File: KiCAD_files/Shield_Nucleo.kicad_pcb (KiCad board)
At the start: 4 copper layers, 100 x 100 mm, 113 parts, among them J1 Conn_01x02, J2 RJ45_LED_Shielded, J3 RJ45_LED_Shielded, J4 Conn_01x02_Male, J5 Conn_01x04_Male, J6 Conn_01x02, J8 Conn_02x07_Odd_Even, SW1 SW_Push, U1 STM32G474RE, U2 AT25xxx, U3 TCAN334GDR, U4 AP1117-33, U5 UCC21222DR, U6 UCC21222DR, U7 SFH617A-2X009T, Y1 NX3225SA-16.000000MHZ-T1

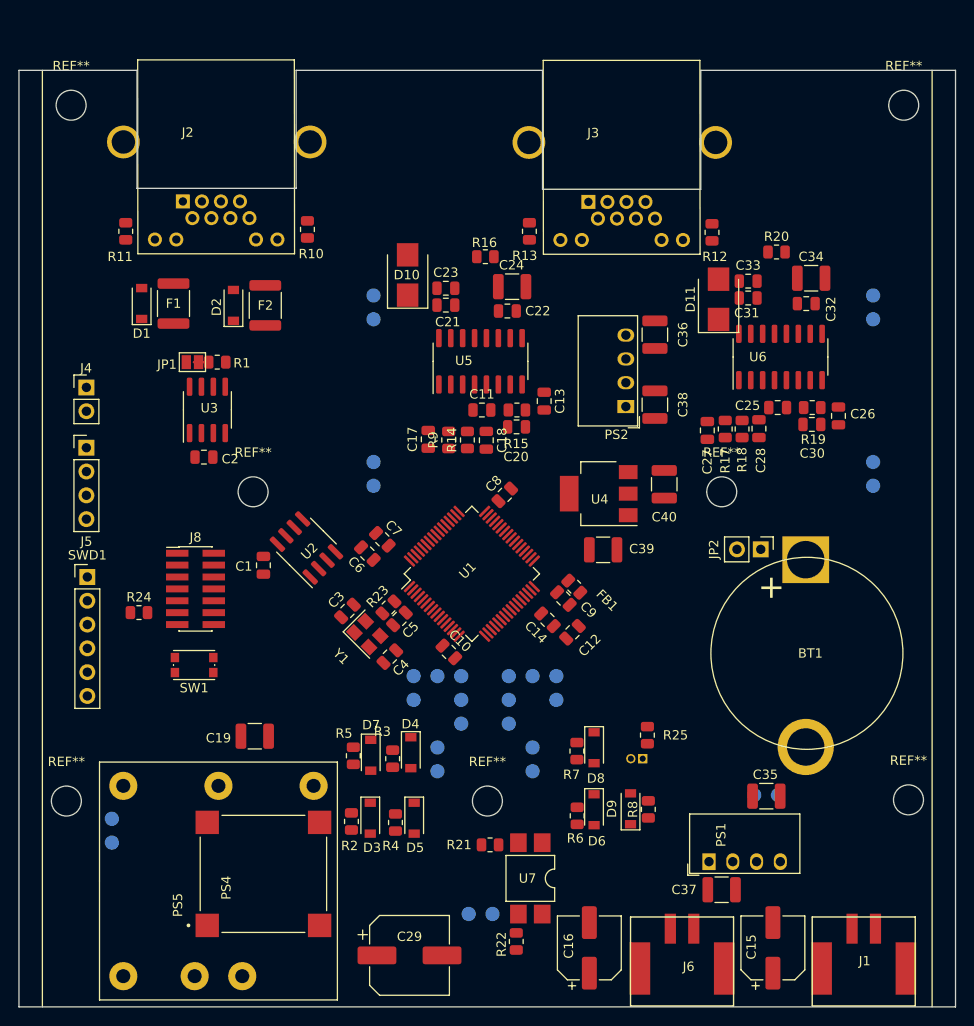
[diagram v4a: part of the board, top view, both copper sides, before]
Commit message: WIP: nearly finished routing - Power need via stiching Signal miss test points connections.
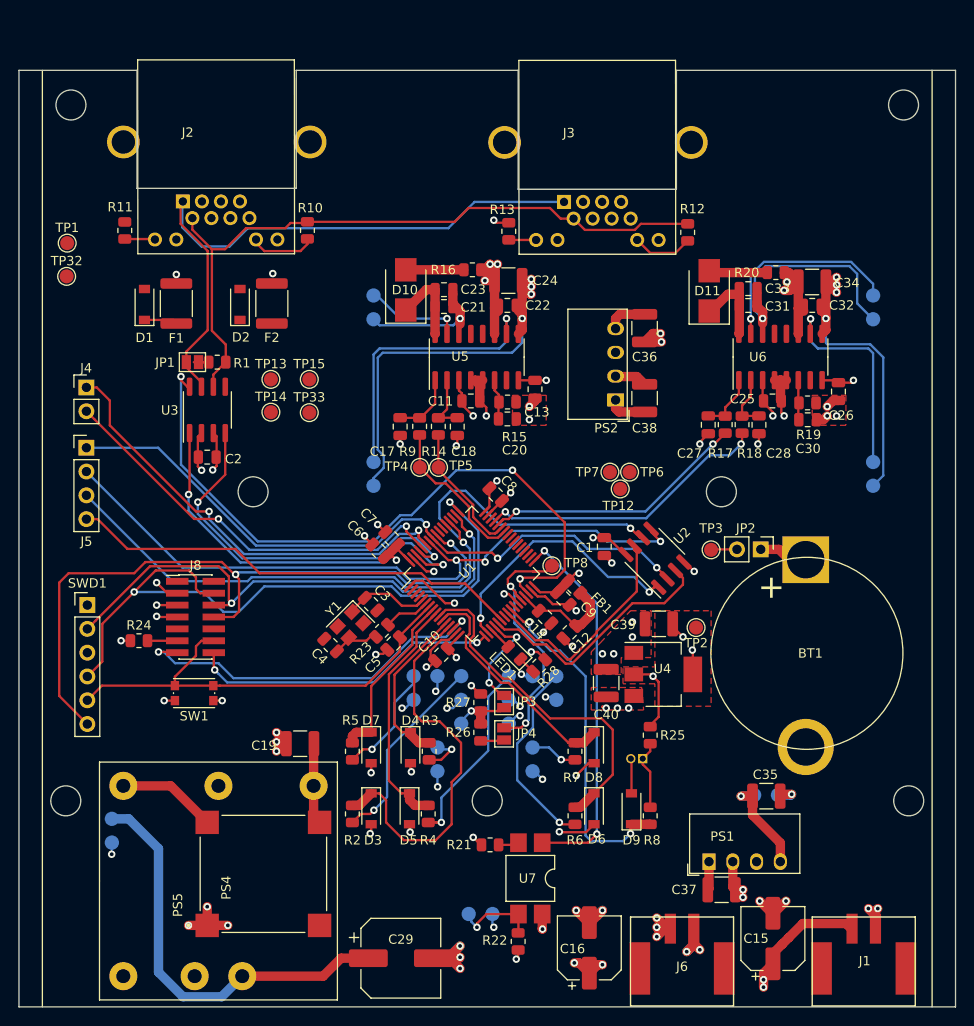
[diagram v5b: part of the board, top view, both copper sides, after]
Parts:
- removed 3D1: 3D_Footprint, Footprints:3D_Footprint_Power
- removed the REF** at (88.5, 104.5)
- removed the REF** at (43.6, 104.5)
- removed the REF** at (113.5, 71.5)
- removed the REF** at (63.5, 71.5)
- removed the REF** at (44.1, 30.2)
- removed the REF** at (133.0, 30.2)
- removed the REF** at (133.5, 104.4)
- added J7: Power, Footprints:3D_Footprint_Power, F.Cu at (38.5, 26.5)
- added JP3: SolderJumper_2_Open, Jumper:SolderJumper-2_P1.3mm_Open_Pad1.0x1.5mm, F.Cu at (90.3, 93.9)
- added JP4: SolderJumper_2_Open, Jumper:SolderJumper-2_P1.3mm_Open_Pad1.0x1.5mm, F.Cu at (90.3, 97.3)
- added LED1: LED, LED_SMD:LED_0805_2012Metric, F.Cu at (91.4, 88.7)
- added R26: 100K, Resistor_SMD:R_0805_2012Metric, F.Cu at (87.8, 97.2)
- added R27: 100K, Resistor_SMD:R_0805_2012Metric, F.Cu at (87.8, 94.0)
- added R28: 330, Resistor_SMD:R_0805_2012Metric, F.Cu at (94.0, 90.1)
- added TP1: TestPoint, TestPoint:TestPoint_Pad_D1.5mm, F.Cu at (43.6, 45.0)
- added TP12: TestPoint, TestPoint:TestPoint_Pad_D1.5mm, F.Cu at (102.7, 71.2)
- added TP13: TestPoint, TestPoint:TestPoint_Pad_D1.5mm, F.Cu at (65.4, 59.5)
- added TP14: TestPoint, TestPoint:TestPoint_Pad_D1.5mm, F.Cu at (65.4, 63.0)
- added TP15: TestPoint, TestPoint:TestPoint_Pad_D1.5mm, F.Cu at (69.5, 59.5)
- added TP2: TestPoint, TestPoint:TestPoint_Pad_D1.5mm, F.Cu at (110.8, 86.0)
- added TP3: TestPoint, TestPoint:TestPoint_Pad_D1.5mm, F.Cu at (112.4, 77.7)
- added TP32: TestPoint, TestPoint:TestPoint_Pad_D1.5mm, F.Cu at (43.6, 48.5)
- added TP33: TestPoint, TestPoint:TestPoint_Pad_D1.5mm, F.Cu at (69.5, 63.0)
- added TP4: TestPoint, TestPoint:TestPoint_Pad_D1.5mm, F.Cu at (81.3, 68.9)
- added TP5: TestPoint, TestPoint:TestPoint_Pad_D1.5mm, F.Cu at (83.3, 68.9)
- added TP6: TestPoint, TestPoint:TestPoint_Pad_D1.5mm, F.Cu at (103.7, 69.4)
- added TP7: TestPoint, TestPoint:TestPoint_Pad_D1.5mm, F.Cu at (101.6, 69.4)
- added TP8: TestPoint, TestPoint:TestPoint_Pad_D1.5mm, F.Cu at (95.4, 79.4)
- moved U2 37.2 mm to (106.4, 78.6)
- moved C1 36.5 mm to (101.0, 77.3)
- moved C40 22.1 mm to (101.2, 91.9)
- moved U4 20.5 mm to (107.3, 91.0), turned to 0 degrees
- moved C39 9.89 mm to (106.8, 85.6), turned to 180 degrees
- moved C4 6.45 mm to (71.8, 87.9), turned to 135 degrees
- moved C19 4.92 mm to (68.5, 98.4)
- moved R3 3.98 mm to (82.3, 99.2)
- moved R4 3.62 mm to (82.2, 105.9)
- moved C18 3.43 mm to (85.3, 64.5)
- moved R14 3.42 mm to (83.3, 64.5)
- moved R9 3.42 mm to (81.3, 64.5)
- moved C17 3.29 mm to (79.2, 64.5)
- moved J8 3.00 mm to (57.4, 84.9)
- moved R24 3.00 mm to (51.3, 87.4)
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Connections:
- net /HRTIM1_CHC1 renamed Net-(U1-Pad34)
- net /HRTIM1_CHC2 renamed Net-(U1-Pad35)
- net /HRTIM1_CHD1 renamed Net-(U1-Pad36)
- net /HRTIM1_CHD2 renamed Net-(U1-Pad37)
- net /HRTIM1_CHE1 renamed Net-(U1-Pad40)
- net /HRTIM1_CHE2 renamed Net-(U1-Pad41)
- net /HRTIM1_CHF1 renamed Net-(U1-Pad38)
- net /HRTIM1_CHF2 renamed Net-(U1-Pad39)
- C15 pad 1: Net-(C15-Pad1) -> /+12VD
- C16 pad 1: Net-(C16-Pad1) -> +12V
- J1 pad 1: Net-(C15-Pad1) -> /+12VD
- J6 pad 1: Net-(C16-Pad1) -> +12V
- PS5 pad 1: Net-(PS5-Pad1) -> /+12VD
- U1 pad 11: /EEPROM_WP -> /V_high_mcu
- U1 pad 13: /V2_low_mcu -> /I1_low_mcu
- U1 pad 19: /V_high_mcu -> /LED_BUILTIN
- U1 pad 20: Net-(U1-Pad20) -> /DAC2
- U1 pad 21: Net-(U1-Pad21) -> /EEPROM_WP
- U1 pad 28: (no net) -> /VREF2048
- U1 pad 8: /I1_low_mcu -> /V2_low_mcu
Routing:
- net GNDD: track 0.00 -> 138.5 mm, vias 0 -> 59
- net GNDREF: track 0.00 -> 110.1 mm, vias 0 -> 18
- net /SPI3_SCK: track 0.00 -> 82.3 mm, vias 0 -> 2
- net /SPI3_MOSI: track 0.00 -> 76.1 mm, vias 0 -> 3
- net /SWO: track 0.00 -> 75.1 mm, vias 0 -> 2
- net /CAN_L: track 0.00 -> 73.9 mm
- net /SWDIO: track 0.00 -> 73.2 mm, vias 0 -> 2
- net /CAN1_STB: track 0.00 -> 72.9 mm, vias 0 -> 3
- net /SPI3_MISO: track 0.00 -> 72.6 mm, vias 0 -> 3
- net /CAN_H: track 0.00 -> 69.0 mm
- net +3V3: track 0.00 -> 60.9 mm, vias 0 -> 10
- net /SWCLK: track 0.00 -> 58.8 mm, vias 0 -> 2
- net /NRST: track 0.00 -> 49.0 mm
- net /SPI3_CS2: track 0.00 -> 48.7 mm
- net /USART1_TX: track 0.00 -> 47.8 mm, vias 0 -> 2
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- added copper zone on In2.Cu, net +12V
- added copper zone on F.Cu, net +3V3
- added copper zone on In2.Cu, net +3V3
- added copper zone on F.Cu, net +5VD
- added copper zone on In2.Cu, net +5VD
- added copper zone on In2.Cu, net /+12VD
- added copper zone on F.Cu, net GNDD
- added copper zone on In1.Cu, net GNDREF
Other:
- outline, holes or cut-outs redrawn

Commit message: WIP: First nightly version of V1.1 - Need verification and validation Possible issue with a current loop on the power PCB...
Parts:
- removed PS1: IA0505S, Converter_DCDC:Converter_DCDC_muRata_CRE1xxxxxx3C_THT
- removed PS2: IA0512S, Converter_DCDC:Converter_DCDC_muRata_CRE1xxxxxx3C_THT
- added U8: RFM-0505s, Converter_DCDC:Converter_DCDC_muRata_CRE1xxxxxx3C_THT, F.Cu at (112.1, 110.8)
- added U9: RFM-0505s, Converter_DCDC:Converter_DCDC_muRata_CRE1xxxxxx3C_THT, F.Cu at (102.2, 61.4)
- TP1, TP12, TP13, TP14, TP15, TP2, TP3, TP32, TP33, TP4, TP5, TP6, TP7, TP8: footprint TestPoint:TestPoint_Pad_D1.5mm -> TestPoint:TestPoint_THTPad_D2.0mm_Drill1.0mm
- moved TP33 31.6 mm to (43.6, 45.0)
- moved TP1 31.5 mm to (69.5, 63.0)
- moved TP8 9.48 mm to (100.2, 71.2)
- moved R23 2.20 mm to (75.6, 87.8)
- moved TP7 1.62 mm to (100.2, 68.5)
- moved TP6 1.14 mm to (103.0, 68.5)
- moved TP4 1.11 mm to (80.2, 69.2)
- moved C38 1.07 mm to (105.6, 60.5), turned to 270 degrees
- moved R14 0.98 mm to (84.2, 64.9)
- moved R9 0.98 mm to (82.2, 64.9)
- moved C18 0.98 mm to (86.2, 64.9)
- moved C17 0.98 mm to (80.1, 64.9)
- moved D11 0.95 mm to (112.2, 51.0)
- moved C5 0.86 mm to (79.2, 88.2)
- moved D10 0.85 mm to (79.8, 50.8)
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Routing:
- net /GND_CAN: track 1.71 -> 106.6 mm, vias 1 -> 3
- net /HRTIM1_CHB1: track 28.3 -> 41.8 mm
- net Net-(D1-Pad1): track 3.56 -> 15.6 mm, vias 0 -> 2
- net /HRTIM1_CHB2: track 31.5 -> 43.5 mm
- net /VREF2048: track 28.4 -> 39.2 mm, vias 2 -> 3
- net /FDCAN1_TX: track 42.9 -> 53.6 mm
- net GNDD: track 138.5 -> 148.6 mm, vias 59 -> 61
- net /CAN1_STB: track 72.9 -> 82.9 mm
- net /V_BUS_CAN: track 0.00 -> 9.18 mm
- net +5V: track 2.80 -> 9.62 mm
- net /FDCAN1_RX: track 40.6 -> 45.5 mm
- net GNDREF: track 110.1 -> 113.2 mm, vias 18 -> 20
- net /HRTIM1_CHA1: track 16.7 -> 19.7 mm
- net +5VD: track 33.1 -> 30.6 mm
- net /HSE_OUT: track 5.02 -> 7.28 mm
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
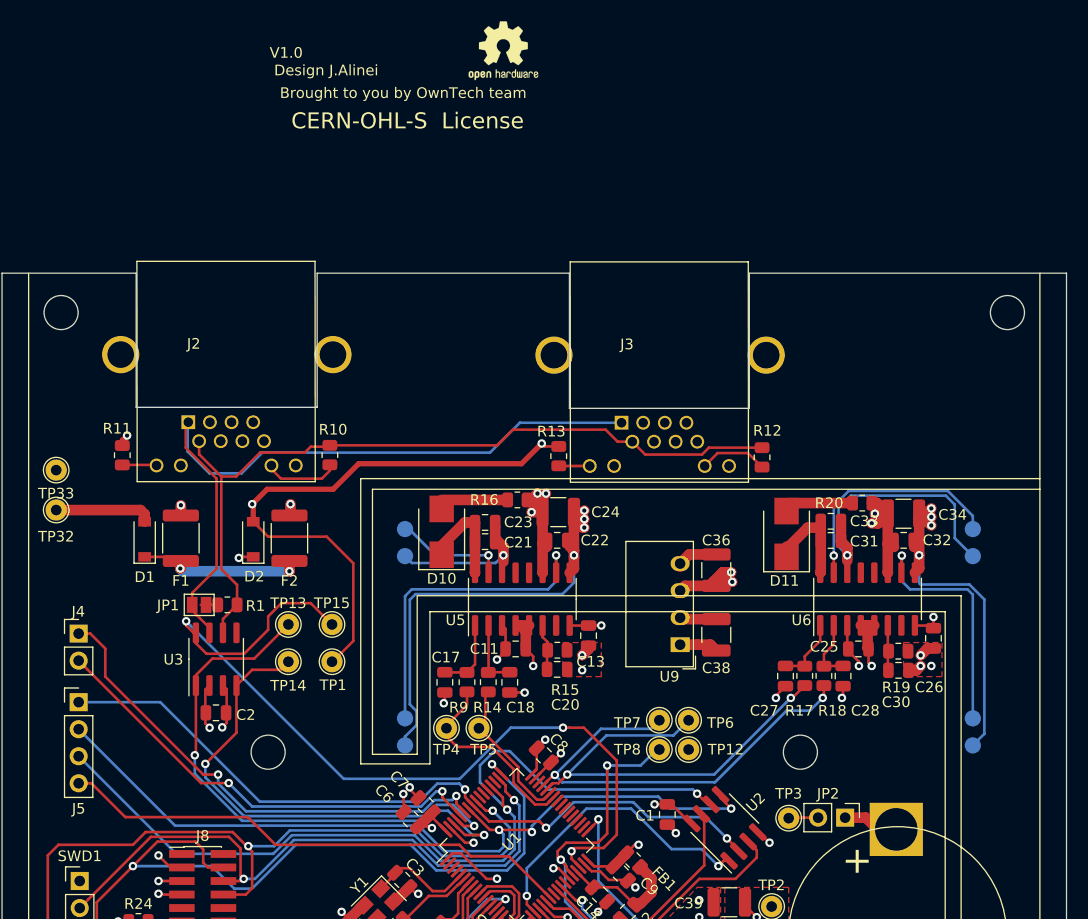
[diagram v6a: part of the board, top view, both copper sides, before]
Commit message: WIP: Corrected small plane mistakes, added GNDREF pin to ext USART and SPI.
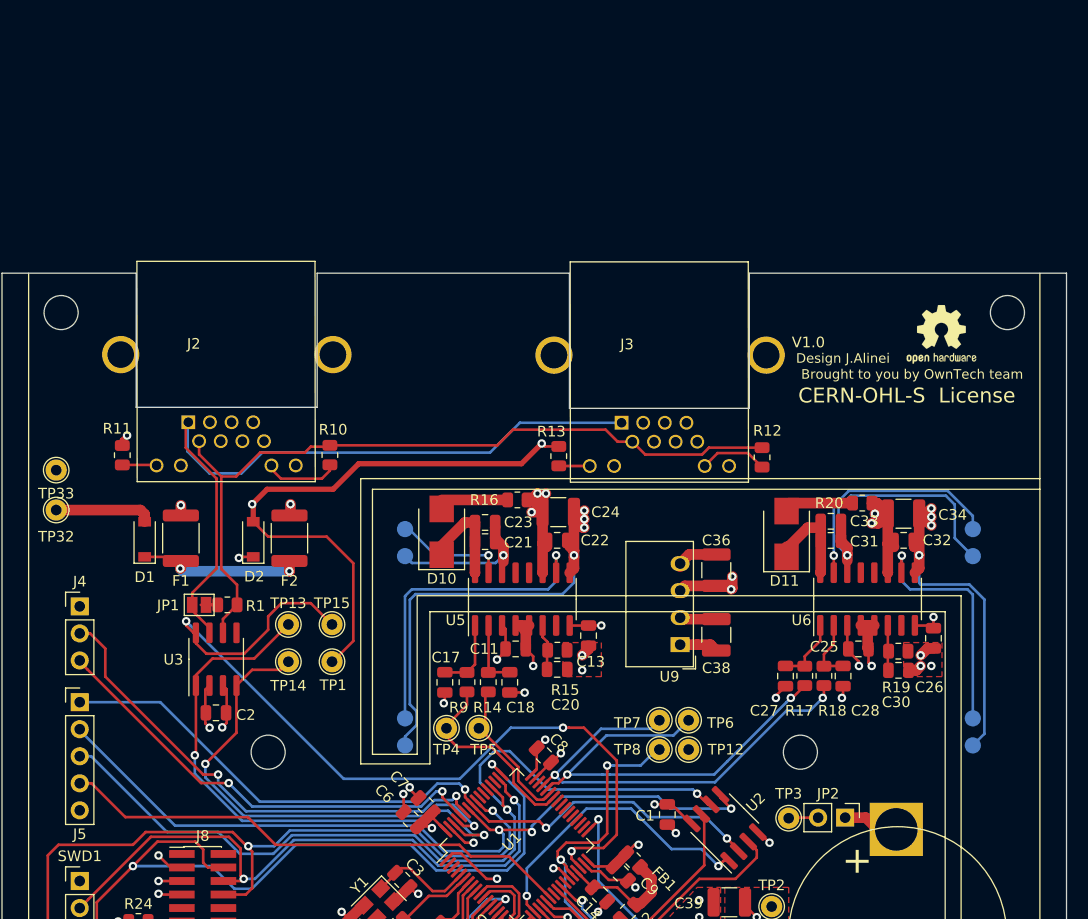
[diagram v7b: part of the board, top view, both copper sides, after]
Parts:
- J4: value Conn_01x02_Male -> Conn_01x03_Male; footprint Connector_PinHeader_2.54mm:PinHeader_1x02_P2.54mm_Vertical -> Connector_PinHeader_2.54mm:PinHeader_1x03_P2.54mm_Vertical
- J5: value Conn_01x04_Male -> Conn_01x05_Male; footprint Connector_PinHeader_2.54mm:PinHeader_1x04_P2.54mm_Vertical -> Connector_PinHeader_2.54mm:PinHeader_1x05_P2.54mm_Vertical
- moved REF** 49.0 mm to (126.8, 32.2)
- moved J4 2.56 mm to (45.8, 57.8)
- moved J5 0.10 mm to (45.8, 66.8)
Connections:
- J4 pad 1: /USART1_TX -> GNDD
- J4 pad 2: /USART1_RX -> /USART1_TX
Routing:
- net GNDREF: track 113.2 -> 110.6 mm
